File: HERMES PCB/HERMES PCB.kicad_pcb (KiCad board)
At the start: 2 copper layers, 99.3 x 118.4 mm, 86 parts

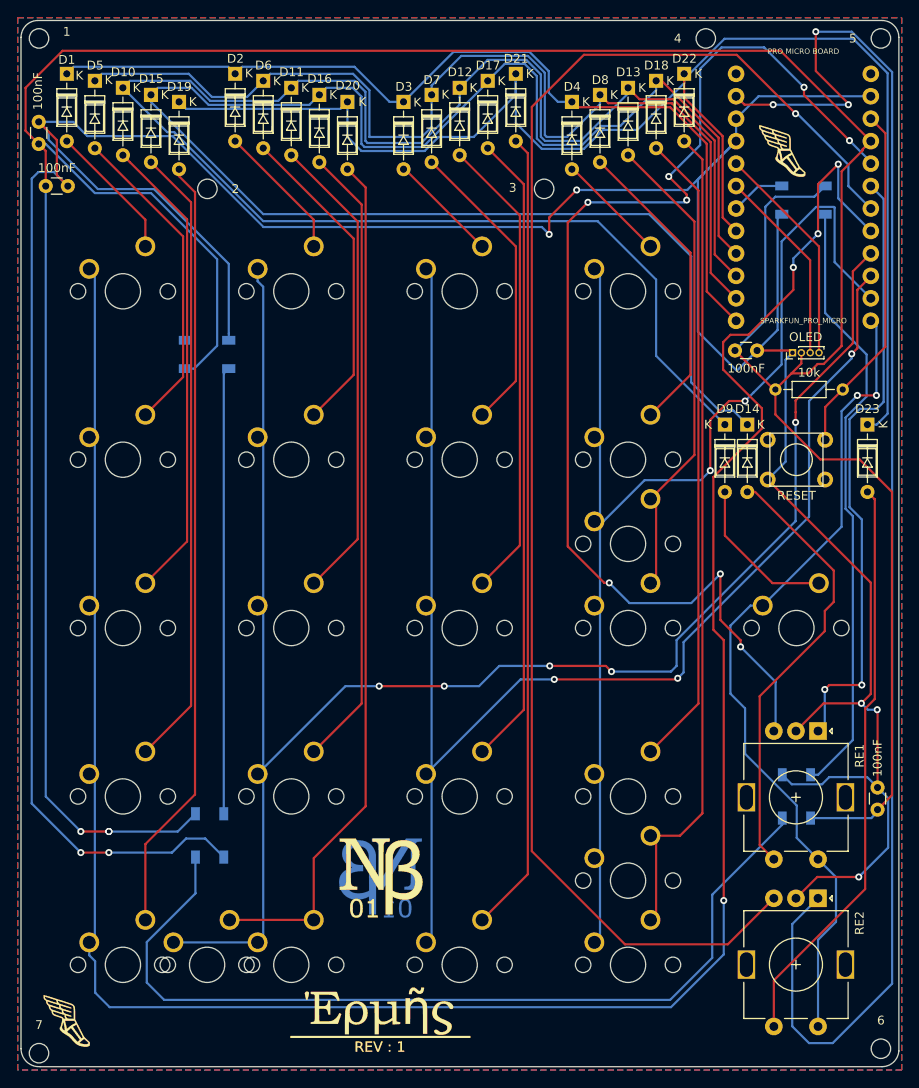
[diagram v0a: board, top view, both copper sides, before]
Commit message: Updated pcb and plate designs, added led difusion layer to chasis
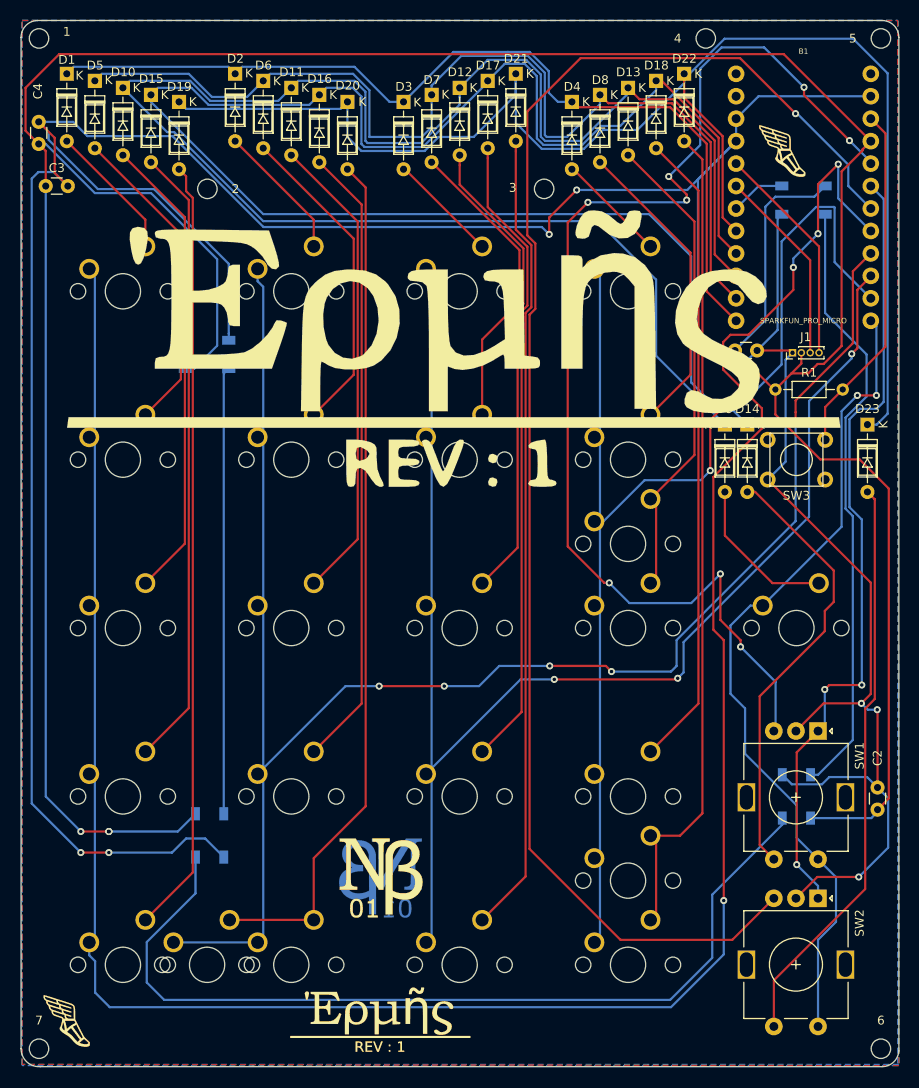
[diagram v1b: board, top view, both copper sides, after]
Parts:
- removed the G*** at (91.9, 153.0) (x2)
- added G***: LOGO, NEWblack:Hermes_big_logo_Fserif, F.Cu at (100.8, 77.0)
- added G***: LOGO, NEWblack:Hermes_big_logo_Fsoldermask, F.Cu at (100.8, 77.0)
- added G***: LOGO, NEWblack:Hermes_big_logo_Fsoldermask, B.Cu at (100.8, 77.0)
- added G***: LOGO, NEWblack:Hermes_big_logo_Fserif, B.Cu at (100.8, 77.0)
- B1: renamed from PRO MICRO BOARD
- moved 7 0.51 mm to (53.2, 156.3)
- renumbered 100nF to C1, 100nF to C2, 100nF to C3, 100nF to C4, OLED to J1, 10k to R1, RE1 to SW1, RE2 to SW2, RESET to SW3
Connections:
- SW2 pad A: D2 -> F5
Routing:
- net D2: track 167.1 -> 0.00 mm, vias 3 -> 0
- net F5: track 69.8 -> 90.7 mm, vias 2 -> 3
- net +5V: track 375.5 -> 374.9 mm

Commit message: minnor changes
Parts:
- removed the G*** at (100.8, 77.0)
